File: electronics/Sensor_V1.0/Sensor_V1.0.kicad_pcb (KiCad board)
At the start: 2 copper layers, 45.9 x 25.6 mm, 33 parts, among them J1 nuclone_small_left, J2 nuclone_small_right, J5 DevBoardUartInput, U1 PPG_sensor, U2 reference_sot23-3

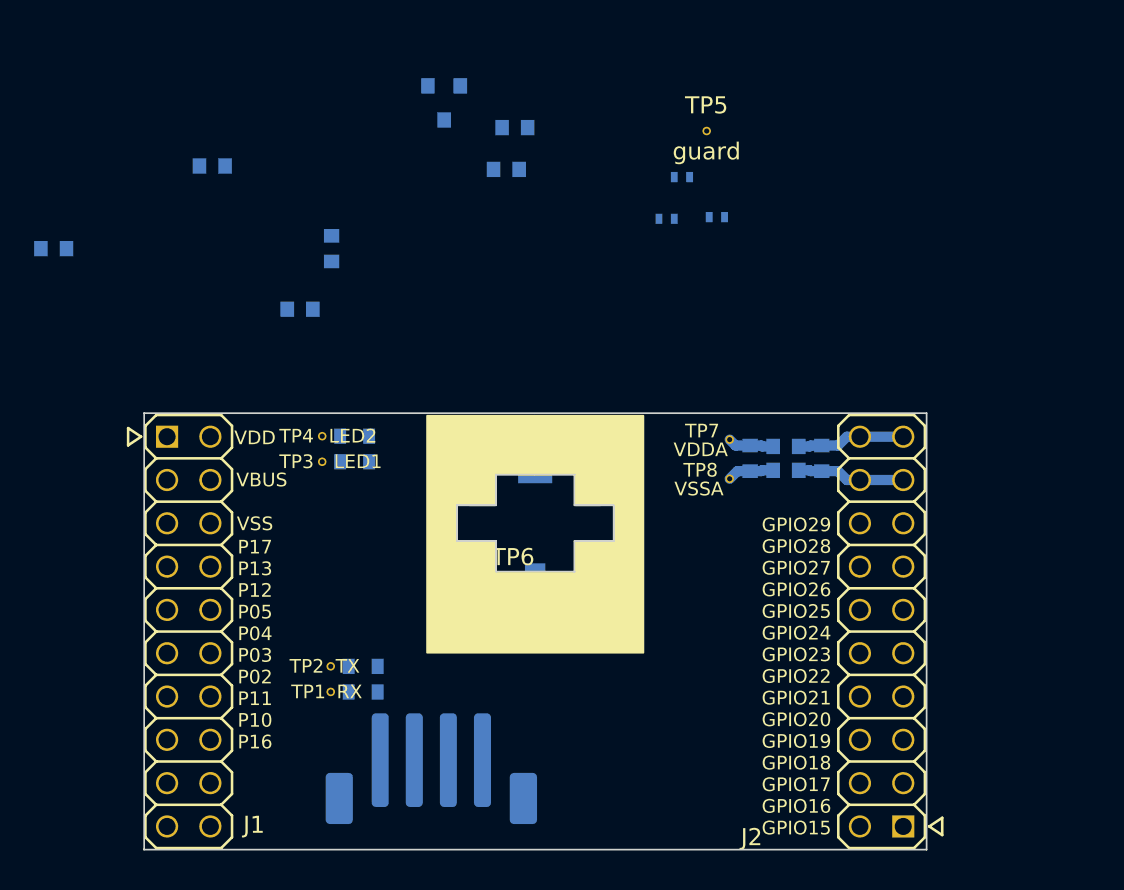
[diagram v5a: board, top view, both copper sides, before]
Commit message: changed some testpads, some futher placement
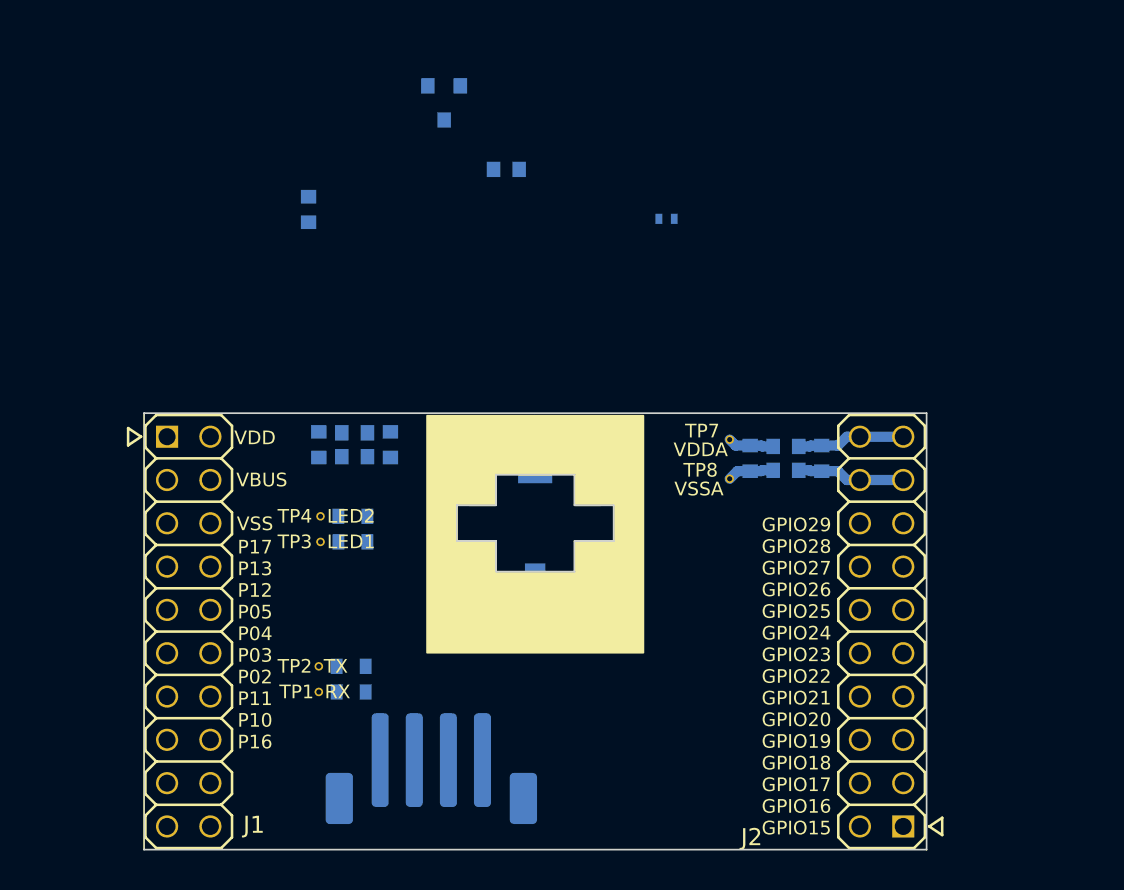
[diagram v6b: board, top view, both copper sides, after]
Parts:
- TP5, TP6: footprint SquantorTestPoints:TestPoint_hole_H03R05 -> SquantorTestPoints:TestPoint_pad_circle_D05; moved to B.Cu
- moved TP5 27.9 mm to (86.4, 83.5)
- moved C3 21.9 mm to (72.4, 75.4), turned to 270 degrees
- moved FB3 20.7 mm to (74.5, 74.7), turned to 180 degrees
- moved JP2 20.3 mm to (79.9, 74.6)
- moved FB4 19.0 mm to (74.5, 76.1)
- moved JP1 13.5 mm to (90.5, 74.5), turned to 180 degrees
- moved C4 9.55 mm to (76.6, 75.4), turned to 270 degrees
- moved R3 4.70 mm to (74.4, 81.1)
- moved R4 4.70 mm to (74.4, 79.6)
- moved TP3 4.70 mm to (72.5, 81.1)
- moved TP4 4.70 mm to (72.5, 79.6)
- moved C6 2.67 mm to (71.8, 61.6)
- moved R1 0.70 mm to (74.3, 89.9)
- moved R2 0.70 mm to (74.3, 88.4)
- moved TP1 0.70 mm to (72.4, 89.9)
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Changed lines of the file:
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@@
     (add_net "Net-(R4-Pad2)")
+  )
+  (module SquantorTestPoints:TestPoint_pad_circle_D05 (layer B.Cu)
+    (at 83.8 83.5)
+    (descr "Test circular pad with 0.5mm diameter")
+    (tags "Test pad 0.5mm")
+    (fp_text reference TP6 (at 0 1.1) (layer B.SilkS)
+      (effects (font (size 1 1) (thickness 0.15)) (justify mirror))
+    )
+    (fp_text value guard (at 0 -1.1) (layer B.SilkS)
+      (effects (font (size 1 1) (thickness 0.15)) (justify mirror))
+    )
+    (fp_circle (center 0 0) (end 0.4 0) (layer B.CrtYd) (width 0.12))
+    (fp_circle (center 0 0) (end 0.4 0) (layer F.CrtYd) (width 0.12))
+    (pad 1 smd circle (at 0 0) (size 0.5 0.5) (layers B.Cu B.Paste B.Mask)
+      (net 49 /PD_OUT_GUARD))
+  )
+  (module SquantorTestPoints:TestPoint_pad_circle_D05 (layer B.Cu)
+    (at 86.4 83.5)
+    (descr "Test circular pad with 0.5mm diameter")
+    (tags "Test pad 0.5mm")
+    (fp_text reference TP5 (at 0 1.1) (layer B.SilkS)
+      (effects (font (size 1 1) (thickness 0.15)) (justify mirror))
+    )
+    (fp_text value guard (at 0 -1.1) (layer B.SilkS)
+      (effects (font (size 1 1) (thickness 0.15)) (justify mirror))
+    )
+    (fp_circle (center 0 0) (end 0.4 0) (layer B.CrtYd) (width 0.12))
+    (fp_circle (center 0 0) (end 0.4 0) (layer F.CrtYd) (width 0.12))
+    (pad 1 smd circle (at 0 0) (size 0.5 0.5) (layers B.Cu B.Paste B.Mask)
+      (net 49 /PD_OUT_GUARD))
   )
   (module SquantorTestPoints:TestPoint_hole_H03R05 (layer F.Cu)
@@
   )
   (module SquantorTestPoints:TestPoint_hole_H03R05 (layer F.Cu)
-    (at 83.8 83.5)
-    (descr "Test point with 0.3mm hole and 0.5mm annular ring")
-    (tags "Test point hole 0.3mm")
-    (fp_text reference TP6 (at 0 -1.5) (layer F.SilkS)
-      (effects (font (size 1 1) (thickness 0.15)))
-    )
-    (fp_text value guard (at 0 1.2) (layer F.SilkS)
-      (effects (font (size 1 1) (thickness 0.15)))
-    )
-    (fp_circle (center 0 0) (end 0.4 0) (layer B.CrtYd) (width 0.12))
-    (fp_circle (center 0 0) (end 0.4 0) (layer F.CrtYd) (width 0.12))
-    (pad 1 thru_hole circle (at 0 0) (size 0.5 0.5) (drill 0.3) (layers *.Cu *.Mask)
-      (net 49 /PD_OUT_GUARD))
-  )
-  (module SquantorTestPoints:TestPoint_hole_H03R05 (layer F.Cu)
-    (at 95.15 57)
-    (descr "Test point with 0.3mm hole and 0.5mm annular ring")
-    (tags "Test point hole 0.3mm")
-    (fp_text reference TP5 (at 0 -1.5) (layer F.SilkS)
-      (effects (font (size 1 1) (thickness 0.15)))
-    )
-    (fp_text value guard (at 0 1.2) (layer F.SilkS)
-      (effects (font (size 1 1) (thickness 0.15)))
-    )
-    (fp_circle (center 0 0) (end 0.4 0) (layer B.CrtYd) (width 0.12))
-    (fp_circle (center 0 0) (end 0.4 0) (layer F.CrtYd) (width 0.12))
-    (pad 1 thru_hole circle (at 0 0) (size 0.5 0.5) (drill 0.3) (layers *.Cu *.Mask)
-      (net 49 /PD_OUT_GUARD))
-  )
-  (module SquantorTestPoints:TestPoint_hole_H03R05 (layer F.Cu)
-    (at 72.6 74.9)
+    (at 72.5 79.6)
     (descr "Test point with 0.3mm hole and 0.5mm annular ring")
     (tags "Test point hole 0.3mm")
@@
   )
   (module SquantorTestPoints:TestPoint_hole_H03R05 (layer F.Cu)
-    (at 72.6 76.4)
+    (at 72.5 81.1)
     (descr "Test point with 0.3mm hole and 0.5mm annular ring")
     (tags "Test point hole 0.3mm")
@@
       (effects (font (size 0.8 0.8) (thickness 0.12)))
     )
-    (fp_text value LED1 (at 2.1 0) (layer F.SilkS)
+    (fp_text value LED1 (at 1.8 0) (layer F.SilkS)
       (effects (font (size 0.8 0.8) (thickness 0.12)))
     )
@@
   )
   (module SquantorTestPoints:TestPoint_hole_H03R05 (layer F.Cu)
-    (at 73.1 88.4)
+    (at 72.4 88.4)
     (descr "Test point with 0.3mm hole and 0.5mm annular ring")
     (tags "Test point hole 0.3mm")
@@
   )
   (module SquantorTestPoints:TestPoint_hole_H03R05 (layer F.Cu)
-    (at 73.1 89.9)
+    (at 72.4 89.9)
     (descr "Test point with 0.3mm hole and 0.5mm annular ring")
     (tags "Test point hole 0.3mm")
@@
   )
   (module SquantorRcl:R_0603_hand (layer B.Cu)
-    (at 74.5 74.9 180)
+    (at 74.4 79.6 180)
     (descr "Resistor SMD 0603, reflow soldering, Vishay (see dcrcw.pdf)")
     (tags "resistor 0603")
@@
   )
   (module SquantorRcl:R_0603_hand (layer B.Cu)
-    (at 74.5 76.4 180)
+    (at 74.4 81.1 180)
     (descr "Resistor SMD 0603, reflow soldering, Vishay (see dcrcw.pdf)")
     (tags "resistor 0603")
@@
   )
   (module SquantorSpecial:solder_jumper_2way_noconn (layer B.Cu)
-    (at 93.7 59.7)
+    (at 79.9 74.6)
     (descr "Resistor SMD 0402, reflow soldering, Vishay (see dcrcw.pdf)")
     (tags "resistor 0402")
@@
   )
   (module SquantorSpecial:solder_jumper_2way_noconn (layer B.Cu)
-    (at 95.75 62.05)
+    (at 90.5 74.5 180)
     (descr "Resistor SMD 0402, reflow soldering, Vishay (see dcrcw.pdf)")
     (tags "resistor 0402")
@@
     (fp_line (start 0.5 -0.25) (end -0.5 -0.25) (layer B.Fab) (width 0.1))
     (fp_line (start -0.5 -0.25) (end -0.5 0.25) (layer B.Fab) (width 0.1))
-    (pad 2 smd rect (at 0.45 0) (size 0.4 0.6) (layers B.Cu B.Mask)
+    (pad 2 smd rect (at 0.45 0 180) (size 0.4 0.6) (layers B.Cu B.Mask)
       (net 44 /PD_BIAS))
-    (pad 1 smd rect (at -0.45 0) (size 0.4 0.6) (layers B.Cu B.Mask)
+    (pad 1 smd rect (at -0.45 0 180) (size 0.4 0.6) (layers B.Cu B.Mask)
       (net 34 /VDDA))
     (model Resistors_SMD.3dshapes/R_0402.wrl
@@
   )
   (module SquantorRcl:L_0603 (layer B.Cu)
-    (at 66.15 59.05 180)
+    (at 74.5 76.1 180)
     (descr "Inductor SMD 0603")
     (tags "Inductor 0402")
@@
   )
   (module SquantorRcl:L_0603 (layer B.Cu)
-    (at 56.85 63.9)
+    (at 74.5 74.7 180)
     (descr "Inductor SMD 0603")
     (tags "Inductor 0402")
@@
     (fp_line (start 0.8 -0.4) (end -0.8 -0.4) (layer B.Fab) (width 0.1))
     (fp_line (start -0.8 -0.4) (end -0.8 0.4) (layer B.Fab) (width 0.1))
-    (pad 2 smd rect (at 0.75 0) (size 0.8 0.9) (layers B.Cu B.Paste B.Mask)
+    (pad 2 smd rect (at 0.75 0 180) (size 0.8 0.9) (layers B.Cu B.Paste B.Mask)
       (net 1 /VBUS))
-    (pad 1 smd rect (at -0.75 0) (size 0.8 0.9) (layers B.Cu B.Paste B.Mask)
+    (pad 1 smd rect (at -0.75 0 180) (size 0.8 0.9) (layers B.Cu B.Paste B.Mask)
       (net 42 "Net-(C4-Pad1)"))
     (model ${KISYS3DMOD}/Inductor_SMD.3dshapes/L_0603_1608Metric.step
@@
   )
   (module SquantorRcl:C_0603 (layer B.Cu)
-    (at 73.15 63.9 270)
+    (at 71.8 61.6 270)
     (descr "Capacitor SMD 0603, reflow soldering, AVX (see smccp.pdf)")
     (tags "capacitor 0603")
@@
   )
   (module SquantorRcl:C_0603 (layer B.Cu)
-    (at 71.3 67.45)
+    (at 76.6 75.4 270)
     (descr "Capacitor SMD 0603, reflow soldering, AVX (see smccp.pdf)")
     (tags "capacitor 0603")
     (attr smd)
-    (fp_text reference C4 (at 0 1.9) (layer B.SilkS)
-      (effects (font (size 1 1) (thickness 0.15)) (justify mirror))
-    )
-    (fp_text value 10u (at 0 -1.9) (layer B.Fab)
+    (fp_text reference C4 (at 0 1.9 90) (layer B.SilkS)
+      (effects (font (size 1 1) (thickness 0.15)) (justify mirror))
+    )
+    (fp_text value 10u (at 0 -1.9 90) (layer B.Fab)
       (effects (font (size 1 1) (thickness 0.15)) (justify mirror))
     )
@@
     (fp_line (start 0.8 -0.4) (end -0.8 -0.4) (layer B.Fab) (width 0.1))
     (fp_line (start -0.8 -0.4) (end -0.8 0.4) (layer B.Fab) (width 0.1))
-    (pad 2 smd rect (at 0.75 0) (size 0.8 0.9) (layers B.Cu B.Paste B.Mask)
+    (pad 2 smd rect (at 0.75 0 270) (size 0.8 0.9) (layers B.Cu B.Paste B.Mask)
       (net 35 /VSSA))
-    (pad 1 smd rect (at -0.75 0) (size 0.8 0.9) (layers B.Cu B.Paste B.Mask)
+    (pad 1 smd rect (at -0.75 0 270) (size 0.8 0.9) (layers B.Cu B.Paste B.Mask)
       (net 42 "Net-(C4-Pad1)"))
     (model ${KISYS3DMOD}/Capacitor_SMD.3dshapes/C_0603_1608Metric.step
@@
   )
   (module SquantorRcl:C_0603 (layer B.Cu)
-    (at 83.9 56.8)
+    (at 72.4 75.4 270)
     (descr "Capacitor SMD 0603, reflow soldering, AVX (see smccp.pdf)")
     (tags "capacitor 0603")
     (attr smd)
-    (fp_text reference C3 (at 0 1.9) (layer B.SilkS)
-      (effects (font (size 1 1) (thickness 0.15)) (justify mirror))
-    )
-    (fp_text value 1u (at 0 -1.9) (layer B.Fab)
+    (fp_text reference C3 (at 0 1.9 90) (layer B.SilkS)
+      (effects (font (size 1 1) (thickness 0.15)) (justify mirror))
+    )
+    (fp_text value 1u (at 0 -1.9 90) (layer B.Fab)
       (effects (font (size 1 1) (thickness 0.15)) (justify mirror))
     )
@@
     (fp_line (start 0.8 -0.4) (end -0.8 -0.4) (layer B.Fab) (width 0.1))
     (fp_line (start -0.8 -0.4) (end -0.8 0.4) (layer B.Fab) (width 0.1))
-    (pad 2 smd rect (at 0.75 0) (size 0.8 0.9) (layers B.Cu B.Paste B.Mask)
+    (pad 2 smd rect (at 0.75 0 270) (size 0.8 0.9) (layers B.Cu B.Paste B.Mask)
       (net 32 /VSS))
-    (pad 1 smd rect (at -0.75 0) (size 0.8 0.9) (layers B.Cu B.Paste B.Mask)
+    (pad 1 smd rect (at -0.75 0 270) (size 0.8 0.9) (layers B.Cu B.Paste B.Mask)
       (net 1 /VBUS))
     (model ${KISYS3DMOD}/Capacitor_SMD.3dshapes/C_0603_1608Metric.step
@@
   )
   (module SquantorRcl:R_0603_hand (layer B.Cu)
-    (at 75 88.4)
+    (at 74.3 88.4)
     (descr "Resistor SMD 0603, reflow soldering, Vishay (see dcrcw.pdf)")
     (tags "resistor 0603")
@@
   )
   (module SquantorRcl:R_0603_hand (layer B.Cu)
-    (at 75 89.9)
+    (at 74.3 89.9)
     (descr "Resistor SMD 0603, reflow soldering, Vishay (see dcrcw.pdf)")
     (tags "resistor 0603")

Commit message: some placement optimizations and minor routing
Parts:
- added C7: 4n7, SquantorRcl:C_0805+0603, B.Cu at (83.1, 86.8)
- added C8: 4n7, SquantorRcl:C_0805+0603, B.Cu at (81.2, 86.8)
- added C9: 4n7, SquantorRcl:C_0805+0603, B.Cu at (85.0, 86.8)
- added JP4: AVDD divider, SquantorSpecial:solder_jumper_2way_noconn, B.Cu at (115.5, 63.9)
- added JP5: VREF divider, SquantorSpecial:solder_jumper_2way_noconn, B.Cu at (115.5, 62.4)
- added Q1: BC846, SquantorIC:SOT23-3, B.Cu at (87.8, 86.8)
- added R10: R, SquantorRcl:R_0603_hand, B.Cu at (110.2, 63.9)
- added R11: 4K7, SquantorRcl:R_0603_hand, B.Cu at (87.4, 90.8)
- added R12: R, SquantorRcl:R_0603_hand, B.Cu at (106.4, 60.9)
- added R13: R, SquantorRcl:R_0603_hand, B.Cu at (106.4, 63.9)
- added R14: R, SquantorRcl:R_0603_hand, B.Cu at (106.4, 62.4)
- added R5: R, SquantorRcl:R_0603_hand, B.Cu at (113.1, 62.4)
- added R6: R, SquantorRcl:R_0603_hand, B.Cu at (113.1, 63.9)
- added R7: R, SquantorRcl:R_0603_hand, B.Cu at (110.2, 60.9)
- added R8: 100K, SquantorRcl:R_0603_hand, B.Cu at (87.4, 89.3)
- added R9: R, SquantorRcl:R_0603_hand, B.Cu at (110.2, 62.4)
- added TP10: PD out, SquantorTestPoints:TestPoint_hole_H03R05, F.Cu at (92.3, 84.8)
- added TP11: Div out, SquantorTestPoints:TestPoint_hole_H03R05, F.Cu at (108.3, 62.4)
- added TP12: I reset, SquantorTestPoints:TestPoint_hole_H03R05, F.Cu at (91.9, 90.2)
- added TP9: guard, SquantorTestPoints:TestPoint_hole_H03R05, F.Cu at (92.3, 83.5)
- moved U2 30.2 mm to (96.8, 80.3), turned to 180 degrees
- moved C6 29.4 mm to (94.3, 80.6), turned to 90 degrees
- moved C5 26.6 mm to (99.2, 80.6), turned to 90 degrees
- moved JP3 13.9 mm to (90.5, 75.9), turned to 180 degrees
- moved J5 2.50 mm to (76.5, 94.4)
- moved JP1 0.10 mm to (90.5, 74.6)
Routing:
- net /PD_OUT_GUARD: track 0.00 -> 30.4 mm
- net /LED2: track 0.00 -> 17.1 mm, vias 0 -> 2
- net /PD_OUT: track 0.00 -> 14.6 mm
- net /PD_BIAS: track 0.00 -> 13.2 mm
- net /LED1: track 0.00 -> 7.94 mm
- net Net-(R4-Pad2): track 0.00 -> 1.05 mm
- net Net-(R3-Pad2): track 0.00 -> 1.05 mm
- net /UART_TX: track 0.00 -> 1.05 mm
- net /UART_RX: track 0.00 -> 1.05 mm
- added copper zone on F.Cu, net /VSS
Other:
- board text added: "P00"
- board text added: "P01"
- board text added: "P06"
- board text added: "P07"
- board text added: "P08"
- board text added: "P09"
- board text added: "P14"
- board text added: "P15"
- board text removed: "GPIO15"
- board text removed: "GPIO16"
- board text removed: "GPIO17"
- board text removed: "GPIO18"
- board text removed: "GPIO19"
- board text removed: "GPIO20"
- board text removed: "GPIO21"
- board text removed: "GPIO22"
- board text removed: "GPIO23"
- board text removed: "GPIO24"
- board text removed: "GPIO25"
- board text removed: "GPIO26"
- board text removed: "GPIO27"
- board text removed: "GPIO28"
- board text removed: "GPIO29"

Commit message: further compaction
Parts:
- J1, J2: moved to B.Cu
- moved TP12 9.49 mm to (99.9, 85.1)
- moved TP9 7.65 mm to (99.9, 82.6)
- moved TP10 7.65 mm to (99.9, 83.9)
- moved N1 7.32 mm to (92.5, 92.2)
- moved N2 7.32 mm to (91.0, 96.2)
- moved N3 7.32 mm to (93.3, 98.2)
- moved TP1 6.87 mm to (70.5, 83.3)
- moved TP2 6.87 mm to (70.5, 81.8)
- moved R1 6.87 mm to (72.4, 83.3)
- moved R2 6.87 mm to (72.4, 81.8)
- moved R11 5.52 mm to (91.9, 87.6), turned to 90 degrees
- moved J5 5.10 mm to (81.6, 94.4)
- moved TP11 4.18 mm to (112.2, 60.9)
- moved R8 3.45 mm to (90.4, 87.6), turned to 270 degrees
- moved R3 2.15 mm to (72.4, 80.3)
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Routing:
- net /LED1: track 7.94 -> 2.40 mm
- net /PD_OUT_GUARD: track 30.4 -> 25.6 mm
- net /LED2: track 17.1 -> 12.6 mm
- net /VSS: track 0.00 -> 3.39 mm, vias 0 -> 2
- net /VSSA: track 2.76 -> 1.37 mm
- net /VDDA: track 2.72 -> 1.37 mm
